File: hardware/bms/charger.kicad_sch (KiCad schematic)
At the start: 65 parts, among them Q7 BSZ018N04LS6ATMA1, Q8 BSZ018N04LS6ATMA1, Q9 BSZ018N04LS6ATMA1, U2 LM74700, U3 BQ24610

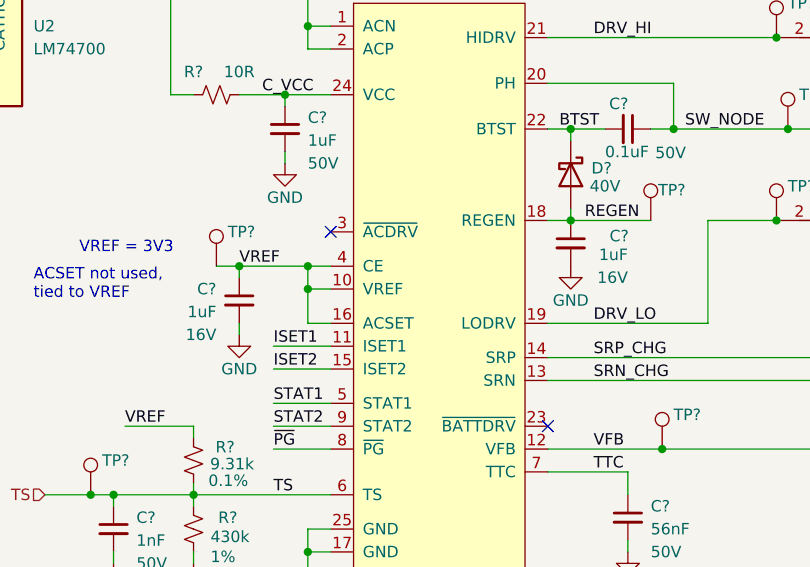
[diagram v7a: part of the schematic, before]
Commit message: Updated MFG PNs, BOM ordered.
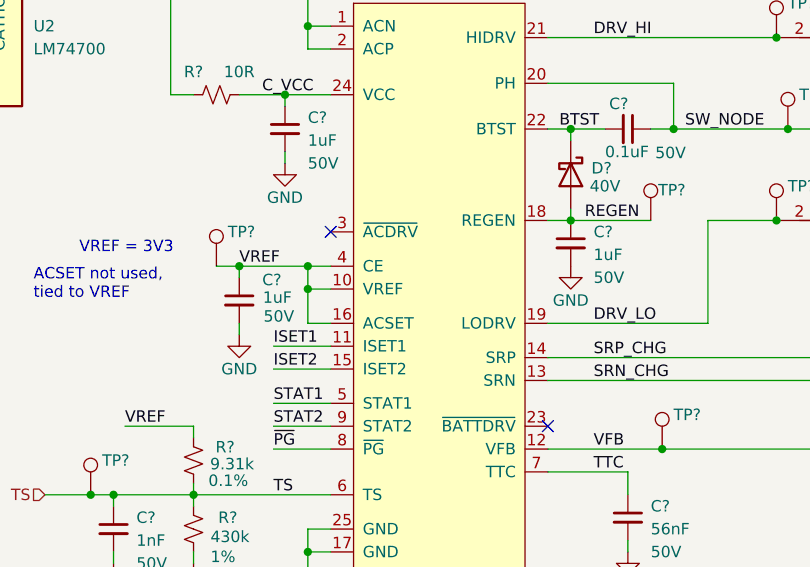
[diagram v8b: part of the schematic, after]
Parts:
- removed C? (x2): 1uF, Capacitor_SMD:C_0603_1608Metric, symbol Device:C_Small
- added C? (x2): 1uF, Capacitor_SMD:C_0603_1608Metric, symbol Device:C_Small
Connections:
- net GND: now also C?.2, C?.2
- net REGEN: now also C?.1
- net VREF: now also C?.1
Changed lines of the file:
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@@
-    )
-  )
-  (symbol (lib_id "Device:C_Small") (at 121.92 85.09 0) (mirror y) (unit 1)
-    (in_bom yes) (on_board yes) (dnp no)
-    (property "Reference" "C?" (at 119.38 83.82 0)
-      (effects (font (size 1.27 1.27)) (justify left))
-    )
-    (property "Value" "1uF" (at 119.38 86.36 0)
-      (effects (font (size 1.27 1.27)) (justify left))
-    )
-    (property "Footprint" "Capacitor_SMD:C_0603_1608Metric" (at 121.92 85.09 0)
-      (effects (font (size 1.27 1.27)) hide)
-    )
-    (property "Datasheet" "~" (at 121.92 85.09 0)
-      (effects (font (size 1.27 1.27)) hide)
-    )
-    (property "MFG" "Murata Electronics" (at 121.92 85.09 0)
-      (effects (font (size 1.27 1.27)) hide)
-    )
-    (property "MFG PN" "GCM188R71C105KA64J" (at 121.92 85.09 0)
-      (effects (font (size 1.27 1.27)) hide)
-    )
-    (property "Voltage" "16V" (at 119.38 88.9 0)
-      (effects (font (size 1.27 1.27)) (justify left))
-    )
-    (pin "1")
-    (pin "2")
-    (instances
-      (project "bms"
-        (path "/a4805e9d-b940-444e-a7cb-db4f4c53ed46/00000000-0000-0000-0000-00006523a805"
-          (reference "C?") (unit 1)
-        )
-        (path "/a4805e9d-b940-444e-a7cb-db4f4c53ed46/00000000-0000-0000-0000-00006523ab32"
-          (reference "C55") (unit 1)
-        )
-      )
     )
   )
@@
     )
   )
+  (symbol (lib_id "Device:C_Small") (at 158.75 78.74 0) (unit 1)
+    (in_bom yes) (on_board yes) (dnp no)
+    (property "Reference" "C?" (at 161.29 77.47 0)
+      (effects (font (size 1.27 1.27)) (justify left))
+    )
+    (property "Value" "1uF" (at 161.29 80.01 0)
+      (effects (font (size 1.27 1.27)) (justify left))
+    )
+    (property "Footprint" "Capacitor_SMD:C_0603_1608Metric" (at 158.75 78.74 0)
+      (effects (font (size 1.27 1.27)) hide)
+    )
+    (property "Datasheet" "~" (at 158.75 78.74 0)
+      (effects (font (size 1.27 1.27)) hide)
+    )
+    (property "MFG" "Murata Electronics" (at 158.75 78.74 0)
+      (effects (font (size 1.27 1.27)) hide)
+    )
+    (property "MFG PN" "GRT188R61H105KE13D" (at 158.75 78.74 0)
+      (effects (font (size 1.27 1.27)) hide)
+    )
+    (property "Voltage" "50V" (at 161.29 82.55 0)
+      (effects (font (size 1.27 1.27)) (justify left))
+    )
+    (pin "1")
+    (pin "2")
+    (instances
+      (project "bms"
+        (path "/a4805e9d-b940-444e-a7cb-db4f4c53ed46/00000000-0000-0000-0000-00006523a805"
+          (reference "C?") (unit 1)
+        )
+        (path "/a4805e9d-b940-444e-a7cb-db4f4c53ed46/00000000-0000-0000-0000-00006523ab32"
+          (reference "C53") (unit 1)
+        )
+      )
+    )
+  )
   (symbol (lib_id "Device:R_Small_US") (at 38.1 151.13 180) (unit 1)
     (in_bom yes) (on_board yes) (dnp no)
@@
         (path "/a4805e9d-b940-444e-a7cb-db4f4c53ed46/00000000-0000-0000-0000-00006523ab32"
           (reference "C58") (unit 1)
-        )
-      )
-    )
-  )
-  (symbol (lib_id "Device:C_Small") (at 158.75 78.74 0) (mirror y) (unit 1)
-    (in_bom yes) (on_board yes) (dnp no)
-    (property "Reference" "C?" (at 165.2048 77.9272 0)
-      (effects (font (size 1.27 1.27)) (justify left))
-    )
-    (property "Value" "1uF" (at 165.1 80.01 0)
-      (effects (font (size 1.27 1.27)) (justify left))
-    )
-    (property "Footprint" "Capacitor_SMD:C_0603_1608Metric" (at 158.75 78.74 0)
-      (effects (font (size 1.27 1.27)) hide)
-    )
-    (property "Datasheet" "~" (at 158.75 78.74 0)
-      (effects (font (size 1.27 1.27)) hide)
-    )
-    (property "MFG" "Murata Electronics" (at 158.75 78.74 0)
-      (effects (font (size 1.27 1.27)) hide)
-    )
-    (property "MFG PN" "GCM188R71C105KA64J" (at 158.75 78.74 0)
-      (effects (font (size 1.27 1.27)) hide)
-    )
-    (property "Voltage" "16V" (at 165.1 82.55 0)
-      (effects (font (size 1.27 1.27)) (justify left))
-    )
-    (pin "1")
-    (pin "2")
-    (instances
-      (project "bms"
-        (path "/a4805e9d-b940-444e-a7cb-db4f4c53ed46/00000000-0000-0000-0000-00006523a805"
-          (reference "C?") (unit 1)
-        )
-        (path "/a4805e9d-b940-444e-a7cb-db4f4c53ed46/00000000-0000-0000-0000-00006523ab32"
-          (reference "C53") (unit 1)
         )
       )
@@
         )
       )
+    )
+  )
+  (symbol (lib_id "Device:C_Small") (at 121.92 85.09 0) (unit 1)
+    (in_bom yes) (on_board yes) (dnp no)
+    (property "Reference" "C?" (at 124.4734 82.8095 0)
+      (effects (font (size 1.27 1.27)) (justify left))
+    )
+    (property "Value" "1uF" (at 124.5432 84.7642 0)
+      (effects (font (size 1.27 1.27)) (justify left))
+    )
+    (property "Footprint" "Capacitor_SMD:C_0603_1608Metric" (at 121.92 85.09 0)
+      (effects (font (size 1.27 1.27)) hide)
+    )
+    (property "Datasheet" "~" (at 121.92 85.09 0)
+      (effects (font (size 1.27 1.27)) hide)
+    )
+    (property "MFG" "Murata Electronics" (at 121.92 85.09 0)
+      (effects (font (size 1.27 1.27)) hide)
+    )
+    (property "MFG PN" "GRT188R61H105KE13D" (at 121.92 85.09 0)
+      (effects (font (size 1.27 1.27)) hide)
+    )
+    (property "Voltage" "50V" (at 124.617 86.8526 0)
+      (effects (font (size 1.27 1.27)) (justify left))
+    )
+    (pin "1")
+    (pin "2")
+    (instances
+      (project "bms"
+        (path "/a4805e9d-b940-444e-a7cb-db4f4c53ed46/00000000-0000-0000-0000-00006523a805"
+          (reference "C?") (unit 1)
+        )
+        (path "/a4805e9d-b940-444e-a7cb-db4f4c53ed46/00000000-0000-0000-0000-00006523ab32"
+          (reference "C55") (unit 1)
+        )
+      )
